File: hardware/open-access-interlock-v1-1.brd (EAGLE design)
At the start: 78.7 x 88.9 mm, 24 parts

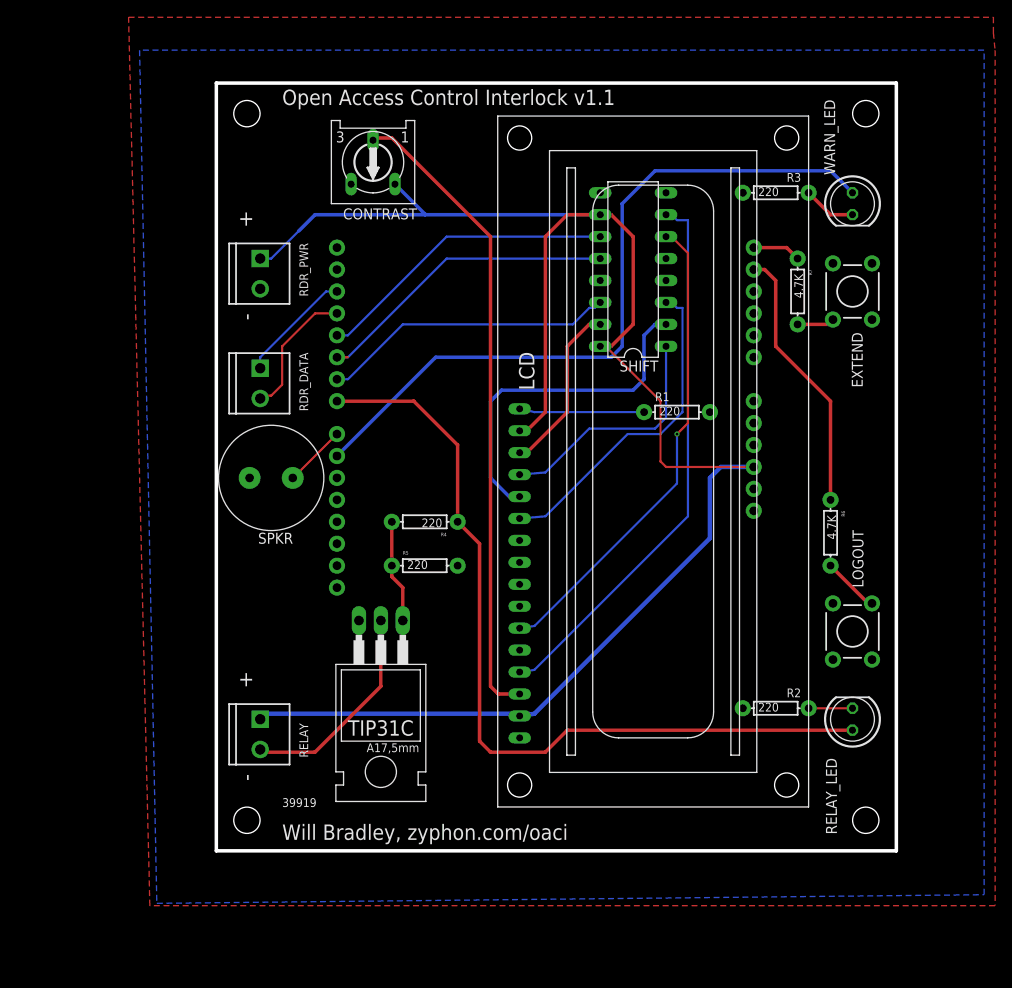
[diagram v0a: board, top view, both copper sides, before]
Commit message: Updated with better screw terminals
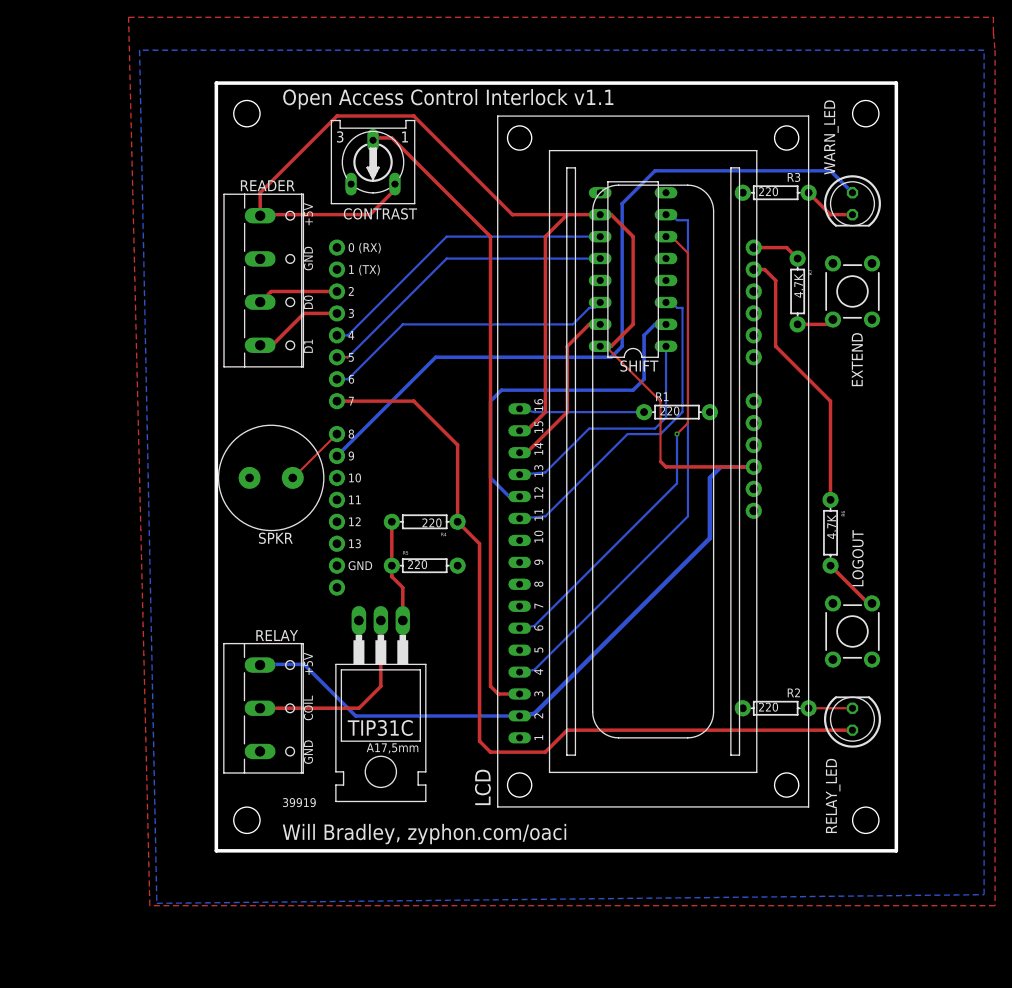
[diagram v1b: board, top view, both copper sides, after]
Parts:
- removed RDR_DATA, RDR_PWR: SCREW, SparkFun:SCREWTERMINAL-3.5MM-2
- added READER: (no value), con-wago-500:W237-4
- RELAY: value SCREW -> (none); device SparkFun:SCREWTERMINAL-3.5MM-2 -> con-wago-500:W237-103
- moved RELAY 1.80 mm to (6.35, 14.0)
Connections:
- net GND: now also READER.2, RELAY.3; no longer RDR_PWR.2
- net N$1: now also READER.3; no longer RDR_DATA.1
- net N$2: now also READER.4; no longer RDR_DATA.2
- net VCC: now also READER.1; no longer RDR_PWR.1
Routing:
- net VCC: track 201.1 -> 220.0 mm
- net N$2: track 15.8 -> 10.4 mm
- net N$1: track 13.3 -> 9.40 mm
- net N$13: track 24.9 -> 22.7 mm
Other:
- board text added: "+5V"
- board text added: "0 (RX)"
- board text added: "1"
- board text added: "1 (TX)"
- board text added: "10"
- board text added: "11"
- board text added: "12"
- board text added: "13"
- board text added: "14"
- board text added: "15"
- board text added: "16"
- board text added: "2"
- board text added: "3"
- board text added: "4"
- board text added: "5"
- board text added: "6"
- board text added: "7"
- board text added: "8"
- board text added: "9"
- board text added: "COIL"
- board text added: "D0"
- board text added: "D1"
- board text added: "GND"
- board text removed: "+"
- board text removed: "-"

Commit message: Final tweaks for terminals and labels
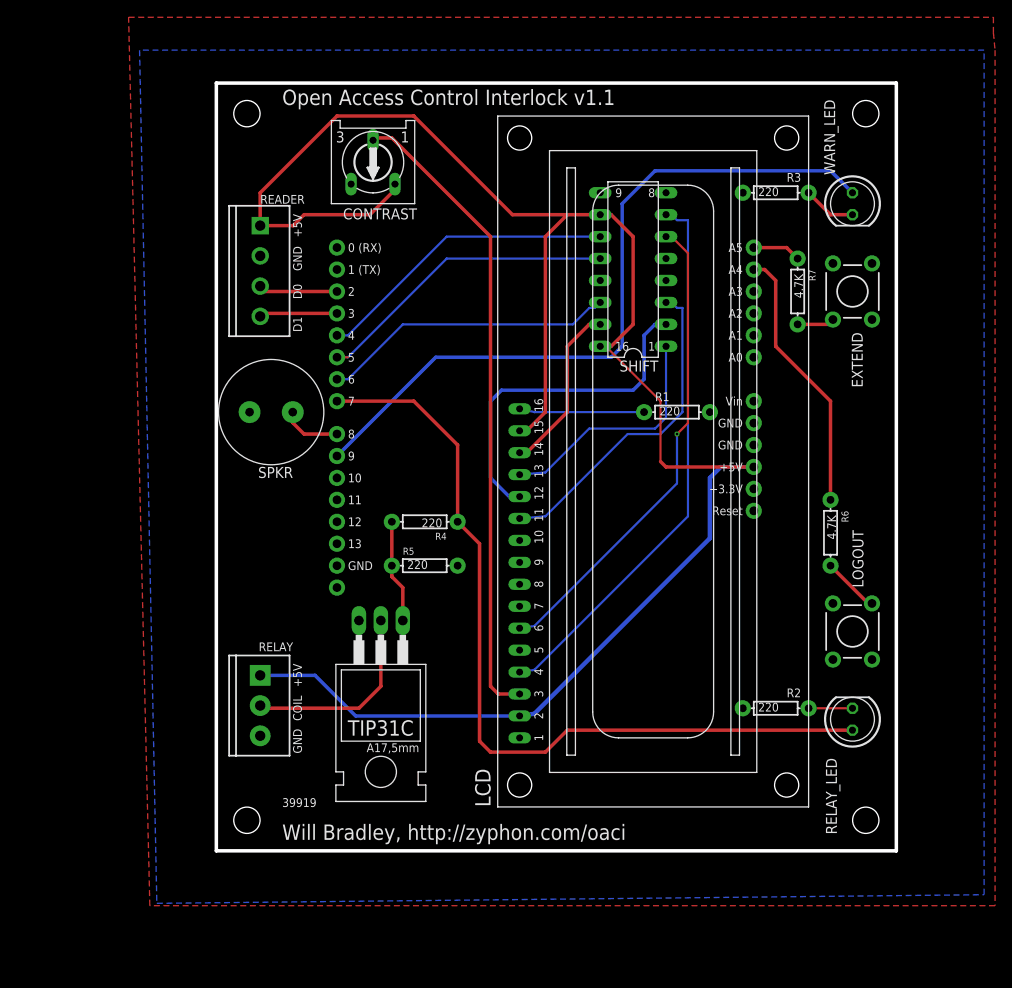
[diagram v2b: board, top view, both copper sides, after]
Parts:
- READER: device con-wago-500:W237-4 -> SparkFun-Connectors:SCREWTERMINAL-3.5MM-4
- RELAY: device con-wago-500:W237-103 -> SparkFun-Connectors:SCREWTERMINAL-3.5MM-3
- moved SPKR 7.62 mm to (6.35, 48.3)
- moved READER 6.48 mm to (5.08, 69.8)
- moved RELAY 4.02 mm to (5.08, 17.8)
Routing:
- net N$2: track 10.4 -> 9.03 mm
- net VCC: track 220.0 -> 221.0 mm
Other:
- board text added: "+3.3V"
- board text added: "A0"
- board text added: "A1"
- board text added: "A2"
- board text added: "A3"
- board text added: "A4"
- board text added: "A5"
- board text added: "Reset"
- board text added: "Vin"
- board text added: "Will Bradley, http://zyphon.com/oaci"
- board text removed: "Will Bradley, zyphon.com/oaci"

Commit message: Fixing transistor/relay stuff
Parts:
- removed TIP31C: TIP30NOHOLE, adafruit:TO220-NOHOLE
- added T1: TIP31, transistor:TO220
- R4: value 220 -> 650ohm
- R5: value 220 -> 6.5K
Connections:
- new net V+: RELAY.1
- new net V-: T1.3
- net GND: no longer RELAY.3, TIP31C.3
- net N$13: now also T1.2; no longer TIP31C.2
- net N$21: now also T1.1; no longer TIP31C.1
- net VCC: no longer RELAY.1
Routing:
- net N$13: track 22.8 -> 15.2 mm
- net VCC: track 221.0 -> 214.7 mm
- net N$21: track 13.2 -> 8.15 mm
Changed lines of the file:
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@@
 <element name="LCD" library="adafruit" package="LCD1602" value="HD44780LCD-1602" x="68.58" y="2.54" smashed="yes" rot="R90"/>
 <element name="SPKR" library="adafruit" package="PS12" value="SPEAKER/PS12" x="6.35" y="48.26" rot="R180"/>
-<element name="TIP31C" library="adafruit" package="TO220-NOHOLE" value="TIP30NOHOLE" x="19.05" y="17.78" smashed="yes" rot="R180">
-<attribute name="NAME" x="22.86" y="12.573" size="1.778" layer="25" ratio="10" rot="R180"/>
-<attribute name="VALUE" x="22.987" y="15.24" size="1.778" layer="27" ratio="10" rot="R180"/>
-</element>
-<element name="R4" library="SparkFun" package="AXIAL-0.3" value="220" x="24.13" y="35.56" smashed="yes" rot="R180">
+<element name="R4" library="SparkFun" package="AXIAL-0.3" value="650ohm" x="24.13" y="35.56" smashed="yes" rot="R180">
 <attribute name="NAME" x="26.67" y="34.29" size="0.8128" layer="25" font="vector" rot="R180"/>
 <attribute name="VALUE" x="26.162" y="35.941" size="1.016" layer="21" font="vector" ratio="15" rot="R180"/>
 </element>
-<element name="R5" library="SparkFun" package="AXIAL-0.3" value="220" x="24.13" y="30.48" smashed="yes">
+<element name="R5" library="SparkFun" package="AXIAL-0.3" value="6.5K" x="24.13" y="30.48" smashed="yes">
 <attribute name="NAME" x="21.59" y="31.75" size="0.8128" layer="25" font="vector"/>
 <attribute name="VALUE" x="22.098" y="30.099" size="1.016" layer="21" font="vector" ratio="15"/>
@@
 <attribute name="VALUE" x="6.35" y="71.12" size="0.4064" layer="27" rot="R270"/>
 </element>
+<element name="T1" library="transistor" package="TO220" value="TIP31" x="-17.78" y="0"/>
 </elements>
 <signals>
@@
 <wire x1="13.97" y1="82.55" x2="5.08" y2="73.66" width="0.4064" layer="1"/>
 <contactref element="READER" pad="1"/>
-<contactref element="RELAY" pad="1"/>
 <wire x1="35.12" y1="13.08" x2="16.13" y2="13.08" width="0.4064" layer="16"/>
 <wire x1="16.13" y1="13.08" x2="11.43" y2="17.78" width="0.4064" layer="16"/>
-<wire x1="11.43" y1="17.78" x2="5.08" y2="17.78" width="0.4064" layer="16"/>
 <wire x1="5.08" y1="73.66" x2="5.08" y2="69.85" width="0.4064" layer="1"/>
 <wire x1="20.685" y1="74.66" x2="20.685" y2="74.025" width="0.4064" layer="1"/>
@@
 <contactref element="SPKR" pad="P$2"/>
 <contactref element="R2" pad="P$1"/>
-<contactref element="TIP31C" pad="3"/>
-<contactref element="R5" pad="P$2"/>
 <contactref element="LCD" pad="1"/>
 <contactref element="R1" pad="P$2"/>
 <contactref element="READER" pad="2"/>
-<contactref element="RELAY" pad="3"/>
+<contactref element="R5" pad="P$2"/>
 </signal>
 <signal name="N$3">
@@
 </signal>
 <signal name="N$13">
-<contactref element="TIP31C" pad="2"/>
-<wire x1="19.05" y1="24.13" x2="19.05" y2="16.51" width="0.4064" layer="1"/>
 <contactref element="RELAY" pad="2"/>
 <wire x1="19.05" y1="16.51" x2="16.51" y2="13.97" width="0.4064" layer="1"/>
 <wire x1="16.51" y1="13.97" x2="5.39" y2="13.97" width="0.4064" layer="1"/>
 <wire x1="5.39" y1="13.97" x2="5.08" y2="14.28" width="0.4064" layer="1"/>
+<contactref element="T1" pad="2"/>
+<wire x1="5.08" y1="14.28" x2="-17.78" y2="-6.35" width="0" layer="19" extent="1-1"/>
 </signal>
 <signal name="N$16">
@@
 <signal name="N$21">
 <contactref element="R4" pad="P$2"/>
-<contactref element="TIP31C" pad="1"/>
 <contactref element="R5" pad="P$1"/>
 <wire x1="20.32" y1="35.56" x2="20.32" y2="30.48" width="0.4064" layer="1"/>
 <wire x1="20.32" y1="30.48" x2="20.32" y2="29.21" width="0.4064" layer="1"/>
 <wire x1="20.32" y1="29.21" x2="21.59" y2="27.94" width="0.4064" layer="1"/>
-<wire x1="21.59" y1="27.94" x2="21.59" y2="24.13" width="0.4064" layer="1"/>
-<wire x1="21.59" y1="22.86" x2="21.59" y2="24.13" width="0.4064" layer="1"/>
+<contactref element="T1" pad="1"/>
+<wire x1="-20.32" y1="-6.35" x2="20.32" y2="29.21" width="0" layer="19" extent="1-1"/>
 </signal>
 <signal name="N$14">
@@
 <wire x1="66.04" y1="67.31" x2="62.23" y2="67.31" width="0.4064" layer="1"/>
 </signal>
+<signal name="V+">
+<contactref element="RELAY" pad="1"/>
+</signal>
+<signal name="V-">
+<contactref element="T1" pad="3"/>
+</signal>
 </signals>
